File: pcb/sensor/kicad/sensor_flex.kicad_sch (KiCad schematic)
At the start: 8 parts, among them J1 CN2 mate (TBD), J2 S7081-42R +5V, J3 S7081-42R GND, U1 SHT45

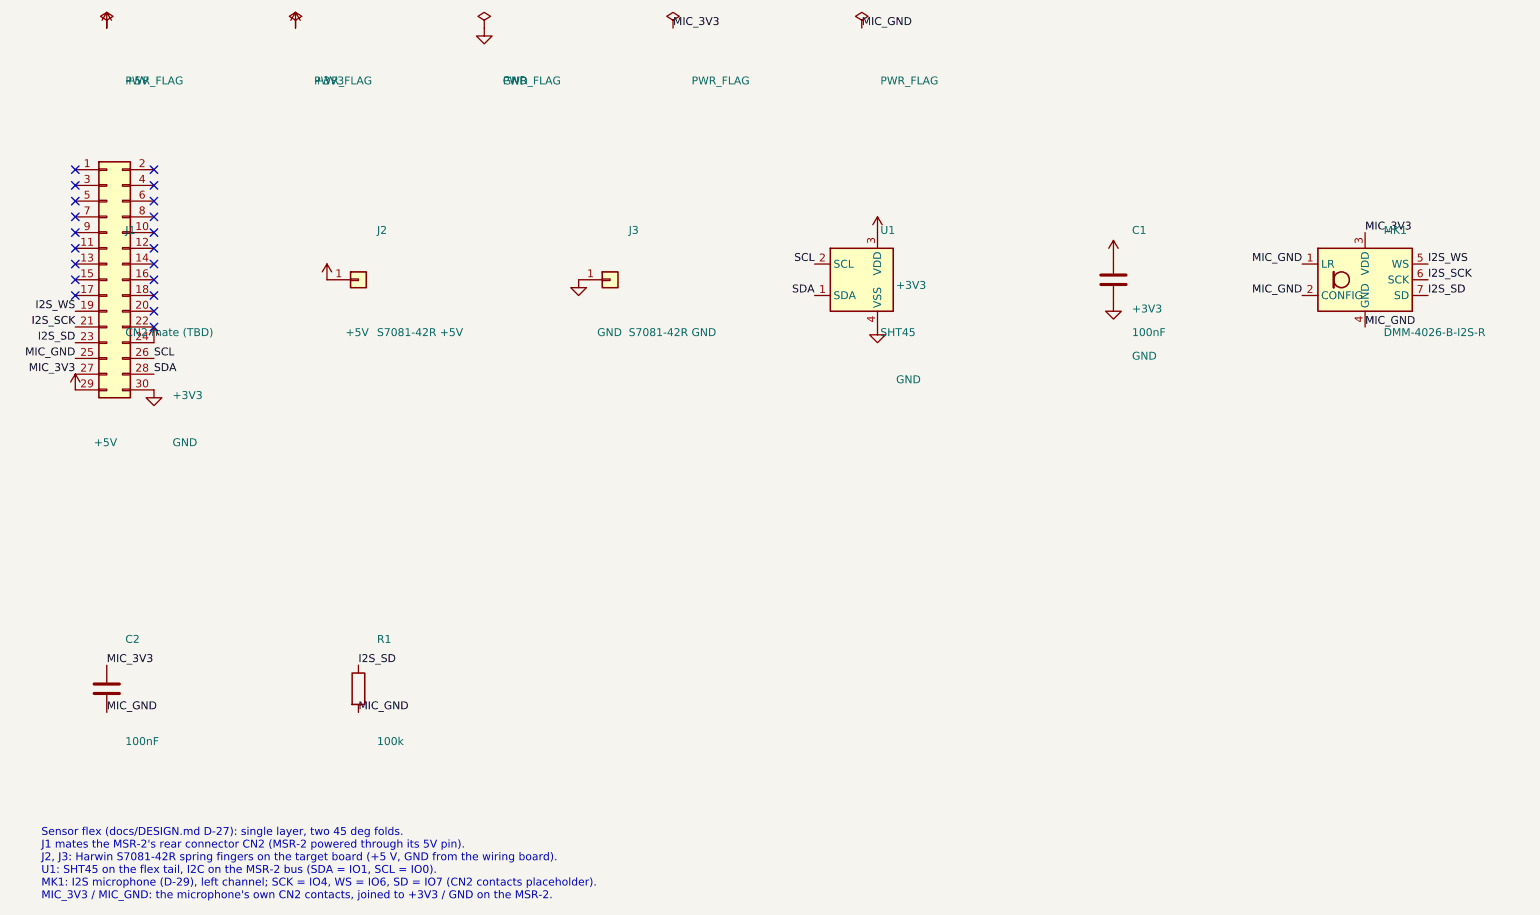
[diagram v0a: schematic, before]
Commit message: Smaller plate, flex ramps and tape points, battery-free tongue on the sensor flex, back cover hooks
- Plate 72 x 132, 5 V contact in the corner, band groove, microphone below the band, two-layer
  sensor flex (D-47)
- Ramps over the flex slopes; tape geometry and tape renders (render_tape.py, D-48)
- Battery-free tongue moved from the 5 V jumper to the sensor flex: under the trim's tab and strip,
  under the floor insert, which hangs from the strip; EU tongue under its floor insert (D-49)
- Back cover: bottom latch 2.9 mm from the edge, end-section snap hooks, notch for the run under
  the GND block; plate clips kept for PETG
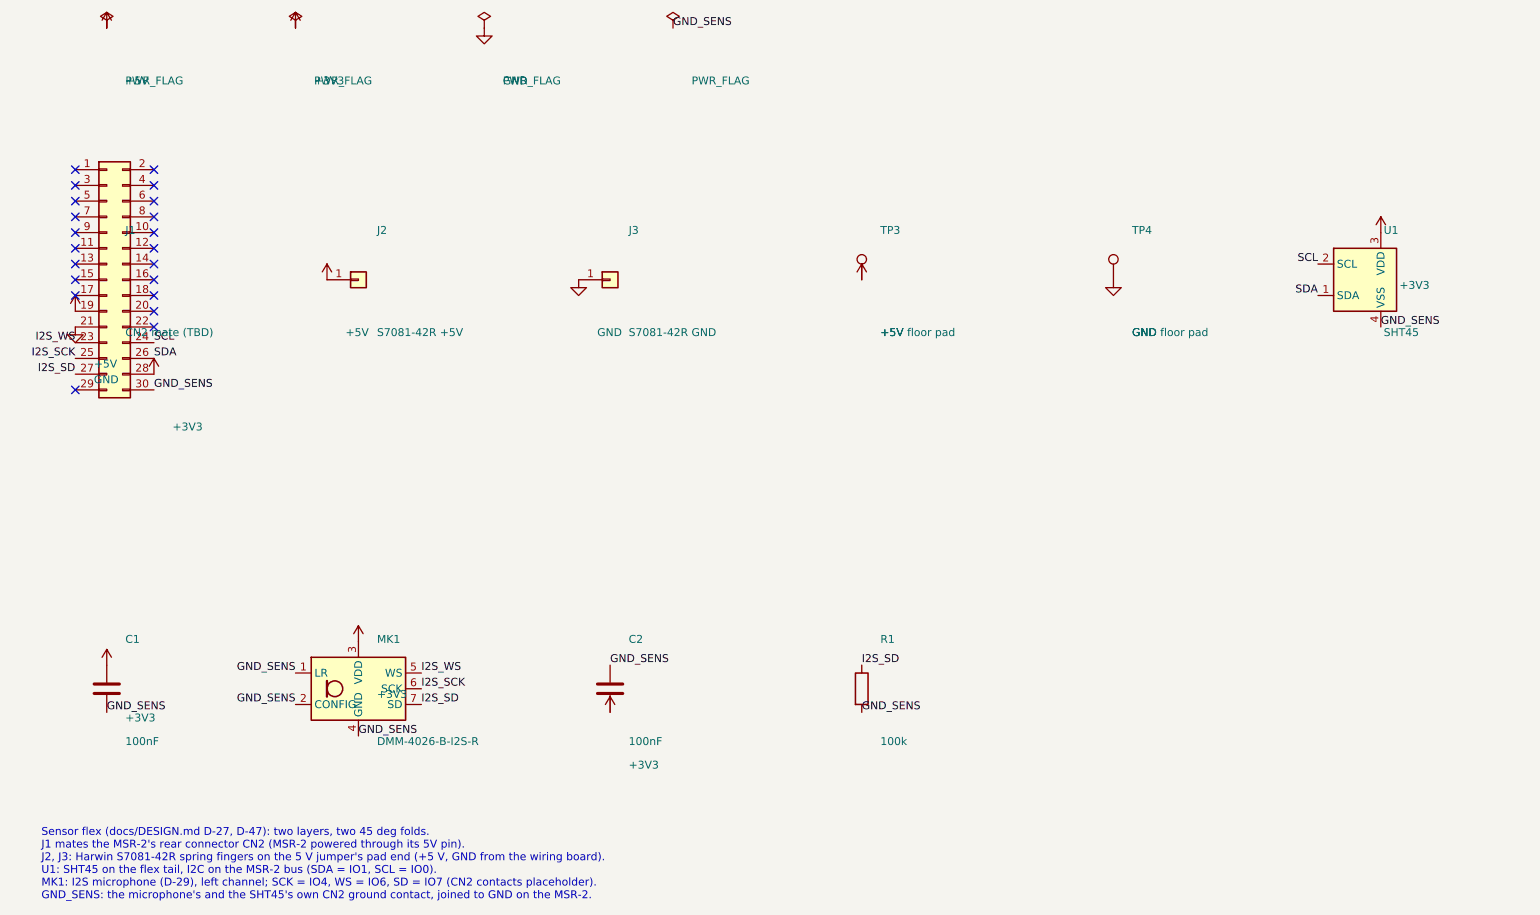
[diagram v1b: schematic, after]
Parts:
- added TP3: +5V floor pad, sensor:Contact_Pad_7x4mm, symbol sensor:TestPoint
- added TP4: GND floor pad, sensor:Contact_Pad_7x4mm, symbol sensor:TestPoint
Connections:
- net +3V3: now also C2.2, J1.28 (Pin_28), MK1.3 (VDD); no longer J1.24 (Pin_24)
- net +5V: now also J1.19 (Pin_19), TP3.1; no longer J1.29 (Pin_29)
- net GND: now also J1.21 (Pin_21), TP4.1; no longer C1.2, J1.30 (Pin_30), U1.4 (VSS)
- net I2S_SCK: now also J1.25 (Pin_25); no longer J1.21 (Pin_21)
- net I2S_SD: now also J1.27 (Pin_27); no longer J1.23 (Pin_23)
- net I2S_WS: now also J1.23 (Pin_23); no longer J1.19 (Pin_19)
- net SCL: now also J1.24 (Pin_24); no longer J1.26 (Pin_26)
- net SDA: now also J1.26 (Pin_26); no longer J1.28 (Pin_28)
- removed net MIC_3V3: C2.1, J1.27 (Pin_27), MK1.3 (VDD)
- net MIC_GND renamed GND_SENS
- net GND_SENS: now also C1.2, C2.1, J1.30 (Pin_30), U1.4 (VSS); no longer C2.2, J1.25 (Pin_25)
- no-connect marks 20 -> 21
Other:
- note added: "Sensor flex (docs/DESIGN.md D-27, D-47): two layers, two 45 deg folds. J1 mates the MSR-2's rear connector CN2 (MSR-2 powered through its 5V pin). J2, J3: Harwin S7081-42R spring fingers on the 5 V jumper's pad end (+5 V, GND from the wiring board). U1: SHT45 on the flex tail, I2C on the MSR-2 bus (SDA = IO1, SCL = IO0). MK1: I2S microphone (D-29), left channel; SCK = IO4, WS = IO6, SD = IO7 (CN2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"
- note removed: "Sensor flex (docs/DESIGN.md D-27): single layer, two 45 deg folds. J1 mates the MSR-2's rear connector CN2 (MSR-2 powered through its 5V pin). J2, J3: Harwin S7081-42R spring fingers on the target board (+5 V, GND from the wiring board). U1: SHT45 on the flex tail, I2C on the MSR-2 bus (SDA = IO1, SCL = IO0). MK1: I2S microphone (D-29), left channel; SCK = IO4, WS = IO6, SD = IO7 (CN2 contacts pl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"
- moved on the sheet: C1, C2, MK1, R1, U1
